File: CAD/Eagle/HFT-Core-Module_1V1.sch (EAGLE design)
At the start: 398 parts, among them Q0521 ABS07-32.768KHZ, Q0811 ABM03B-32.000MHZ, Q0911 ABM3B-16MHZ-10-R50-1-U, T1201 MMBT2222, T1202 MMBT2222, T1203 MMBT2222, U0111 STM32L4Z_144PIN_SMPS, U0431 PAM2305AAB120, U0601 LM4120IM5-3.0, U0611 MAX5217, U0631 CFPT-141-20MHZ, U0641 OPA354, U0701 Si5338, U0801 SX1276, U0901 AX5243, U0911 PE4259, U0921 PE4259, U0991 PE4259, U1101 MCP3911A0-E-SS, U1111 MAX5136AGTG+, U1121 OPA354, U1131 OPA354, U1141 OPA354, U1201 NHD-C0220BIZ_2X20CHARS, U1301 MPU-9250, U1311 MS5607-02BA03, U1321 SHT31-DIS, U1402 SPV1040T, U1501 TS5A23166, U1601 SC189ZSKTRT, U1701 TS5A23166, U1801 TS5A23166, U1901 TS5A23166, X1261 TTE_EN11-HSM, X1401 WIRE-TO-BOARD_5MM08_1X02, X2001 MOLEX 105017-0001, X2101 SMA_SMT_AMPHENOL-901-143, SAM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, X2111 SMA_SMT_AMPHENOL-901-143, SAM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, X2201 CUI SJ1-3535NS, X2211 CUI SJ1-3535NS, X2311 2X20/90_1MM27_HARWIN_M50-3202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, X2312 2X20/90_1MM27_HARWIN_M50-3202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, X2321 2X20/90_1MM27_HARWIN_M50-3202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, X2322 2X20/90_1MM27_HARWIN_M50-3202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, X2331 2X20/90_1MM27_HARWIN_M50-3202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, X2332 2X20/90_1MM27_HARWIN_M50-3202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

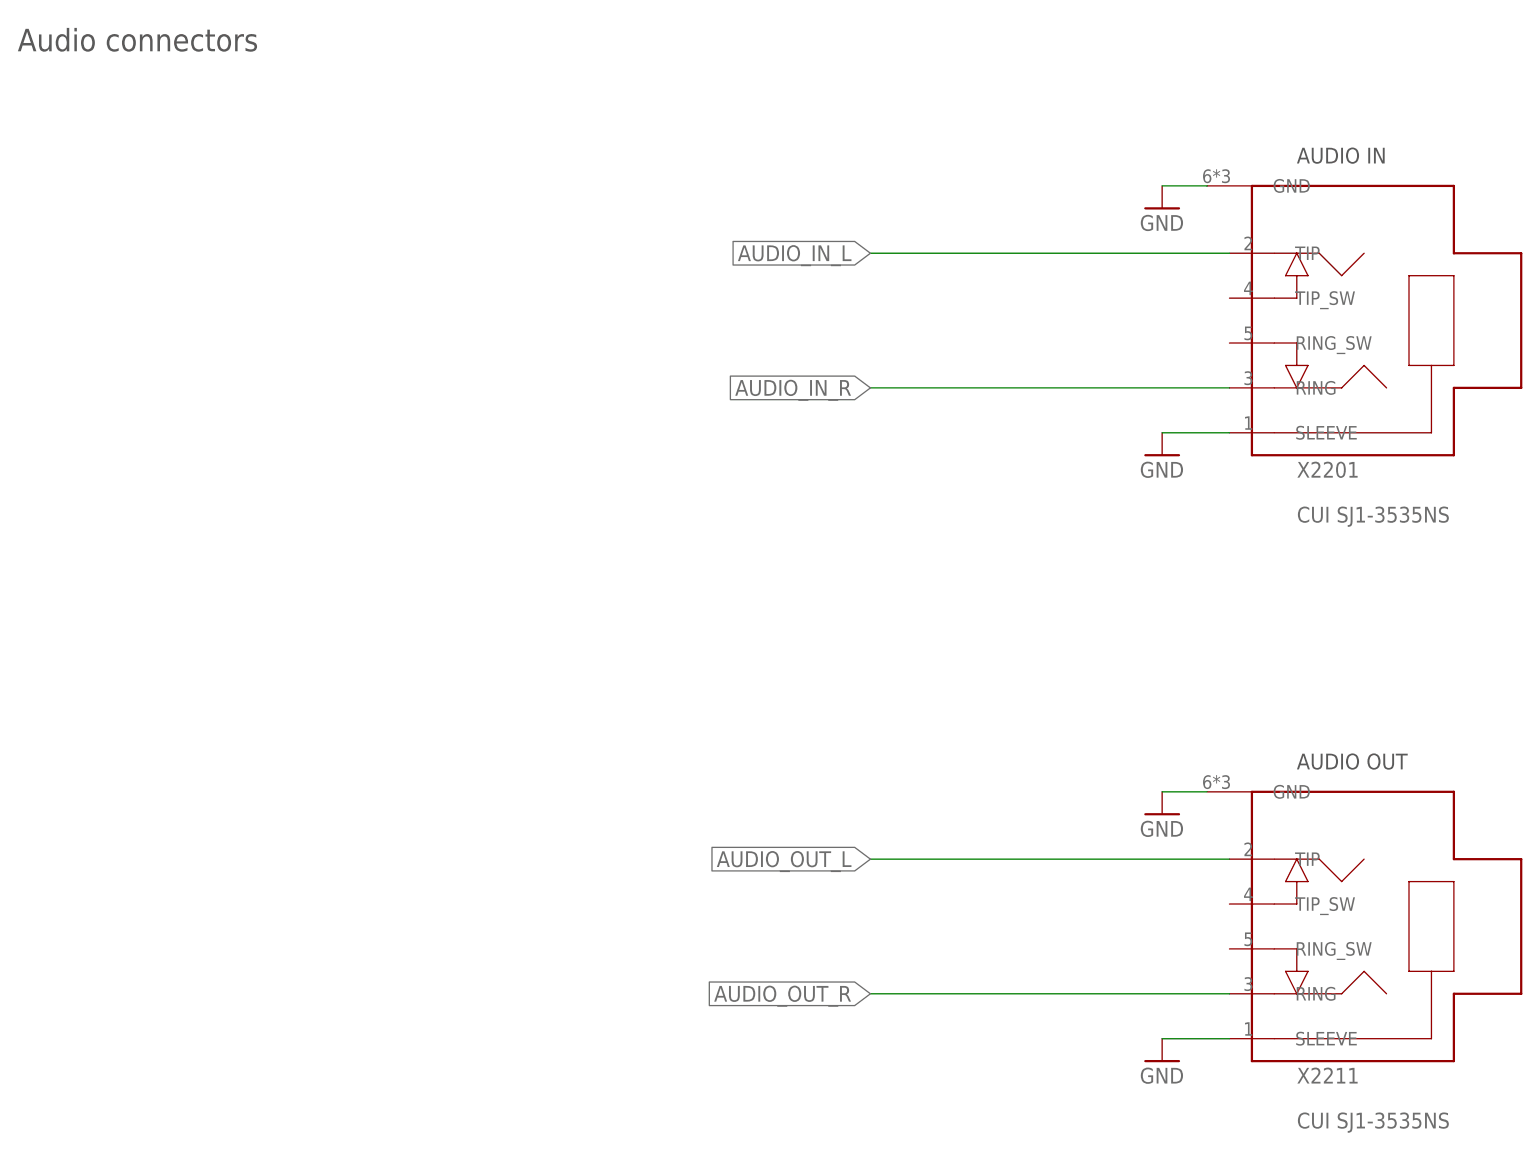
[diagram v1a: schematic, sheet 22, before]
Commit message: HW_1V1 - CAD/Eagle - LCD, Audio jacks and Rotary encoder corrected
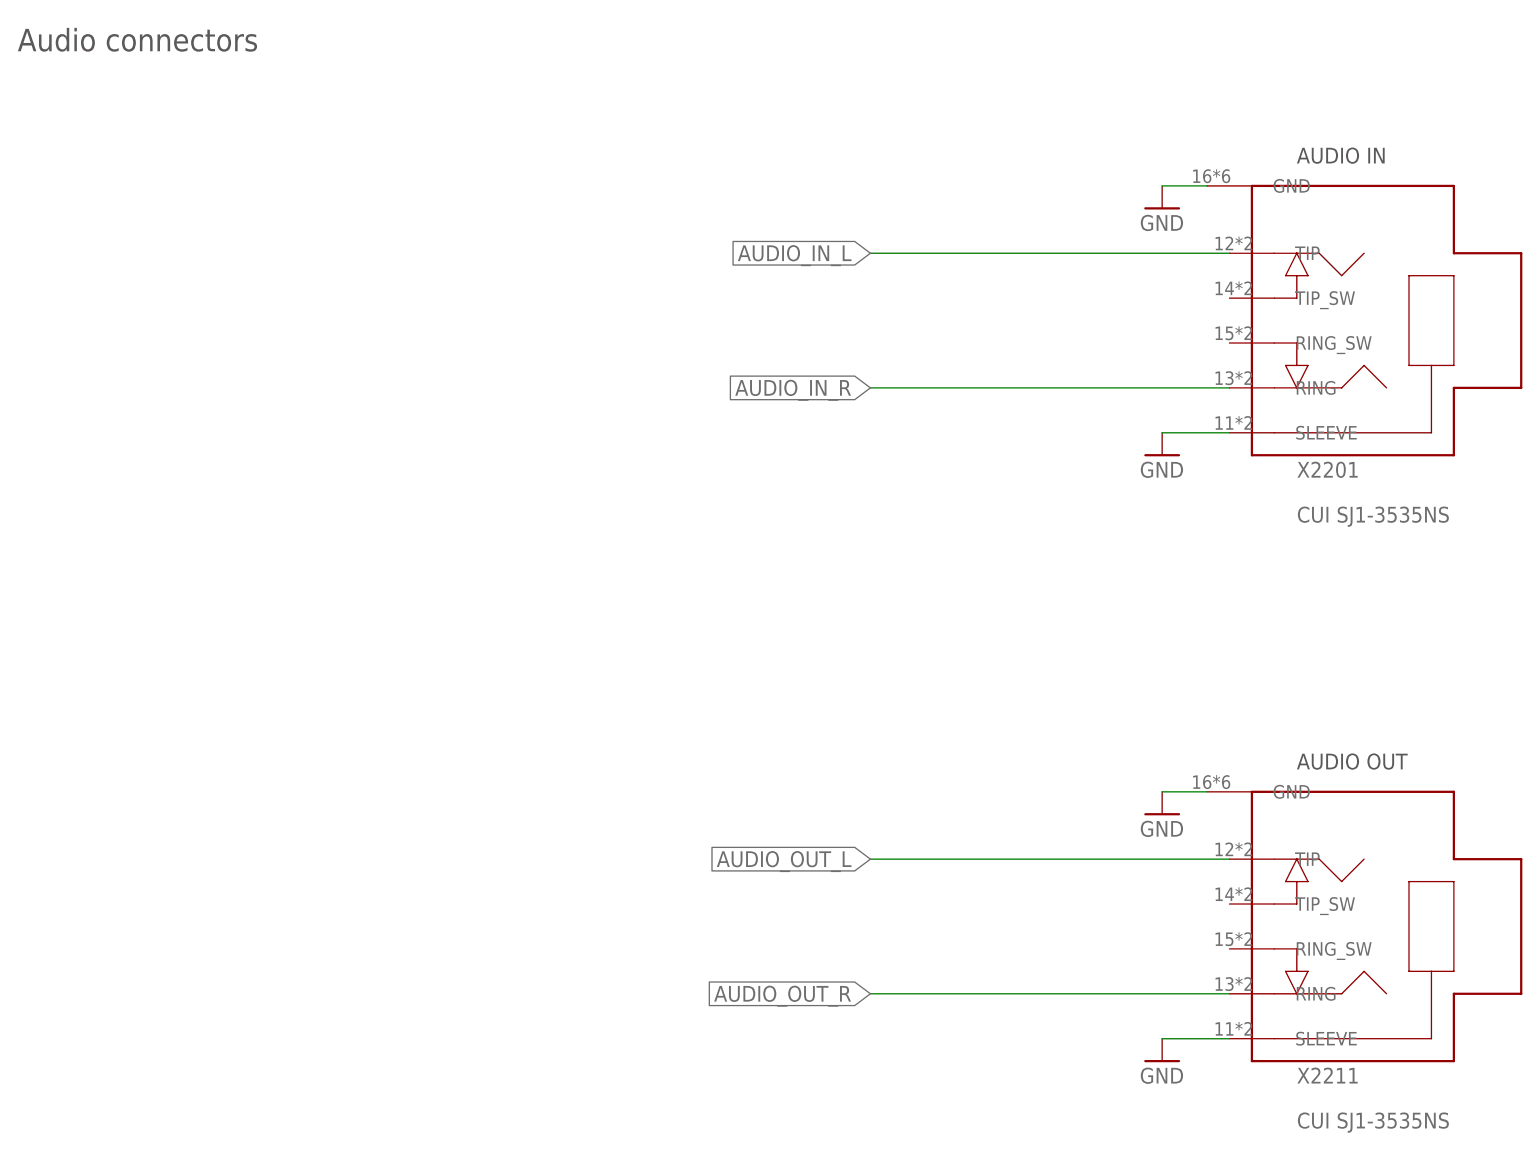
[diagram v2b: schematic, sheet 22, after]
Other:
- moved on the sheet: U1201, X2201, X2211

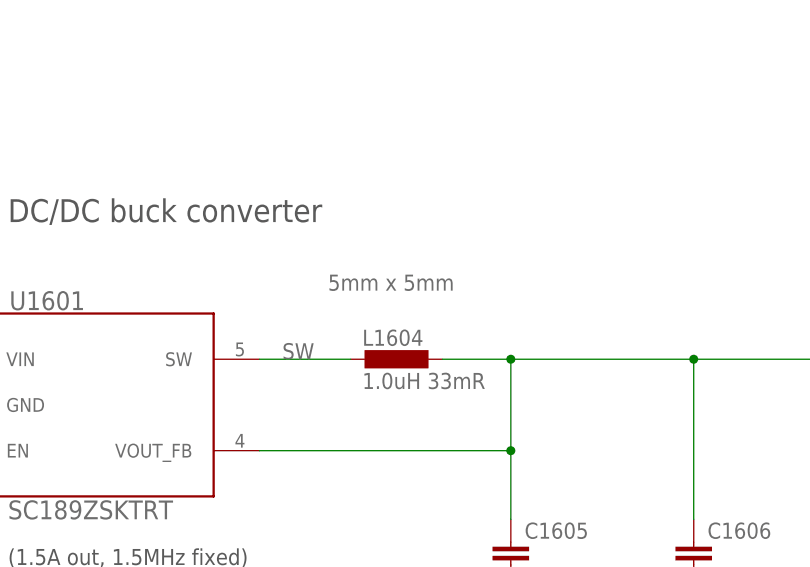
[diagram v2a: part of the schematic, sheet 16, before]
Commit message: HW_1V1 - CAD/Eagle - L1604 size reduced to 3mm x 3mm
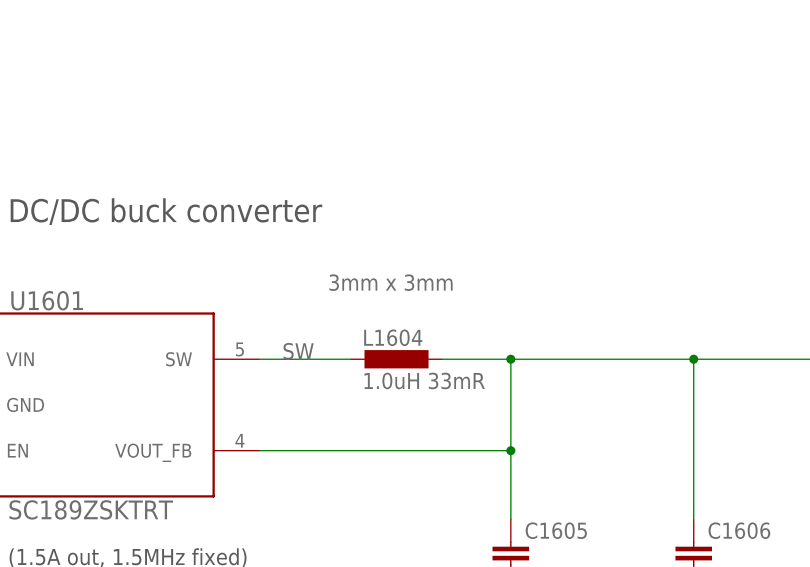
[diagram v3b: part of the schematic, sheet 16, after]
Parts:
- L1604: device rcl:L-EUL5650M -> df4iah_rcl:L-EUL3230M
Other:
- note added: "3mm x 3mm"
- note removed: "5mm x 5mm"
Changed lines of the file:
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@@
 <part name="X2331" library="df4iah_connector" deviceset="2X20/90_1MM27_HARWIN_M50-3202045" device=""/>
 <part name="C1602" library="rcl" deviceset="C-EU" device="C0805" value="47uF"/>
-<part name="L1604" library="rcl" deviceset="L-EU" device="L5650M" value="1.0uH 33mR"/>
+<part name="L1604" library="df4iah_rcl" deviceset="L-EU" device="L3230M" value="1.0uH 33mR"/>
 <part name="C1605" library="rcl" deviceset="C-EU" device="C0603" value="100nF"/>
 <part name="C1606" library="rcl" deviceset="C-EU" device="C0805" value="47uF"/>
@@
 <description>5V -&gt; 3V3</description>
 <plain>
-<text x="139.7" y="104.14" size="1.778" layer="96">5mm x 5mm</text>
+<text x="139.7" y="104.14" size="1.778" layer="96">3mm x 3mm</text>
 <text x="104.14" y="111.76" size="2.54" layer="97" ratio="15">DC/DC buck converter</text>
 <text x="22.86" y="162.56" size="2.54" layer="97" ratio="15">Power converter 5V --&gt; 3.3V</text>

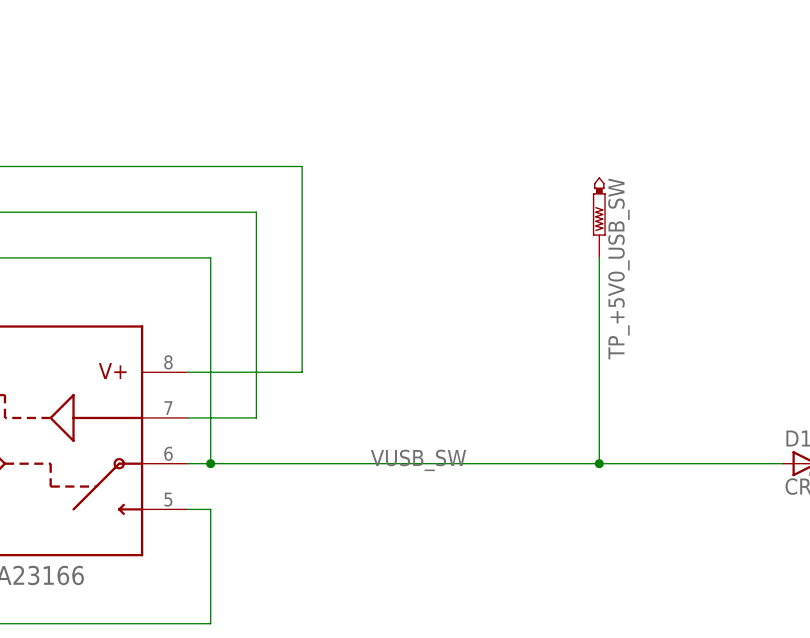
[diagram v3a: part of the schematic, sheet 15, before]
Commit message: HW_1V1 - CAD/Eagle - USB power switch bridged by 50R to enable power-up
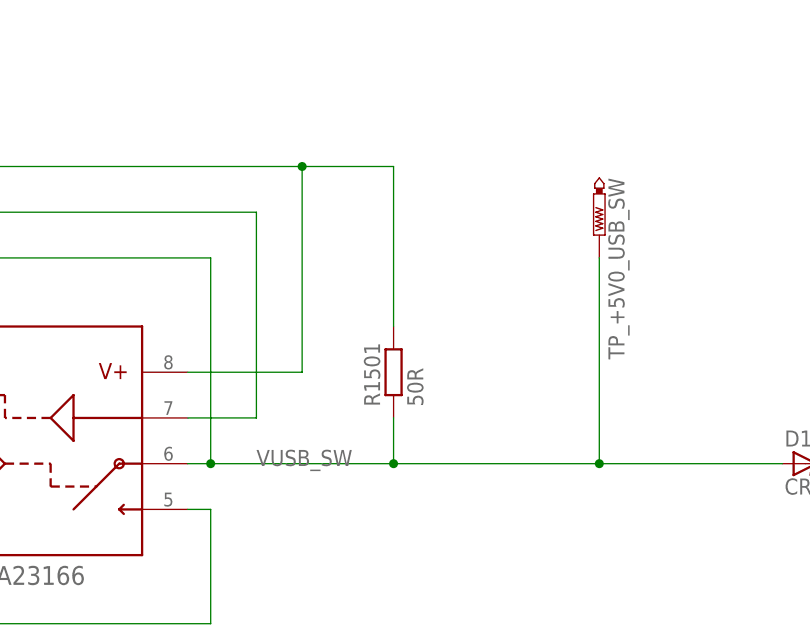
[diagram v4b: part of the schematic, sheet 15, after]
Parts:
- added R1501: 50R, df4iah_rcl:R-EU_R0805
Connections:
- net VDDUSB: now also R1501.2
- net VUSB_SW: now also R1501.1
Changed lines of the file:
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@@
 <part name="R1412" library="rcl" deviceset="R-EU_" device="R0603" value="100kR"/>
 <part name="X1401" library="df4iah_connector" deviceset="WIRE-TO-BOARD_5MM08_1X02" device=""/>
+<part name="R1501" library="df4iah_rcl" deviceset="R-EU_" device="R0805" value="50R"/>
 </parts>
 <sheets>
@@
 <instance part="C1501" gate="G$1" x="68.58" y="71.12"/>
 <instance part="R1502" gate="G$1" x="83.82" y="71.12" rot="R90"/>
+<instance part="R1501" gate="G$1" x="154.94" y="96.52" rot="R90"/>
 </instances>
 <busses>
@@
 <wire x1="198.12" y1="86.36" x2="177.8" y2="86.36" width="0.1524" layer="91"/>
 <pinref part="D1501" gate="G$1" pin="A"/>
-<label x="152.4" y="86.106" size="1.778" layer="95"/>
-<wire x1="177.8" y1="86.36" x2="134.62" y2="86.36" width="0.1524" layer="91"/>
+<label x="139.7" y="86.106" size="1.778" layer="95"/>
+<wire x1="177.8" y1="86.36" x2="154.94" y2="86.36" width="0.1524" layer="91"/>
+<wire x1="154.94" y1="86.36" x2="134.62" y2="86.36" width="0.1524" layer="91"/>
 <wire x1="134.62" y1="109.22" x2="134.62" y2="86.36" width="0.1524" layer="91"/>
 <wire x1="134.62" y1="109.22" x2="93.98" y2="109.22" width="0.1524" layer="91"/>
@@
 <wire x1="177.8" y1="86.36" x2="177.8" y2="109.22" width="0.1524" layer="91"/>
 <junction x="177.8" y="86.36"/>
+<pinref part="R1501" gate="G$1" pin="1"/>
+<wire x1="154.94" y1="86.36" x2="154.94" y2="91.44" width="0.1524" layer="91"/>
+<junction x="154.94" y="86.36"/>
 </segment>
 </net>
@@
 <wire x1="68.58" y1="96.52" x2="68.58" y2="73.66" width="0.1524" layer="91"/>
 <junction x="68.58" y="96.52"/>
+<wire x1="144.78" y1="119.38" x2="154.94" y2="119.38" width="0.1524" layer="91"/>
+<pinref part="R1501" gate="G$1" pin="2"/>
+<wire x1="154.94" y1="119.38" x2="154.94" y2="101.6" width="0.1524" layer="91"/>
+<junction x="144.78" y="119.38"/>
 </segment>
 </net>

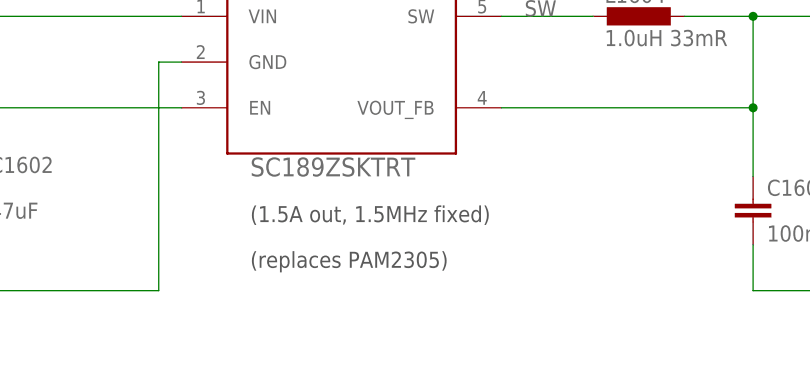
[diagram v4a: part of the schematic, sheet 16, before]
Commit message: HW_1V1 - CAD/Eagle - notice added about current consumption of DcDc converters
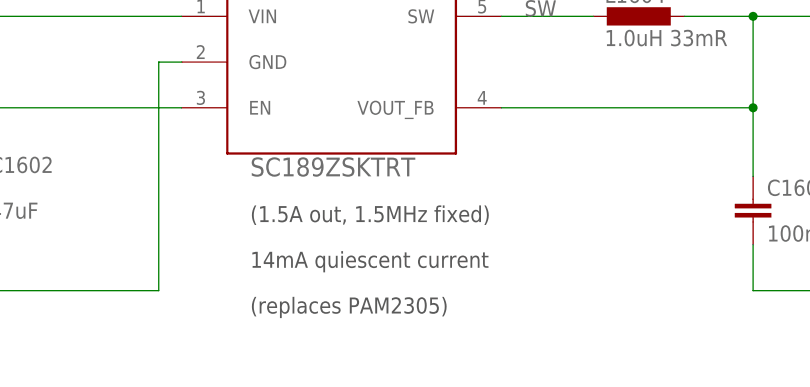
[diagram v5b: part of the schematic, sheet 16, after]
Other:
- note added: "12mA Start-up mode 2mA MPPT mode"
- note added: "14mA quiescent current"
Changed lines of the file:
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@@
 <text x="30.48" y="139.7" size="1.778" layer="97">MCU_VSOL_TIMCAP</text>
 <text x="10.16" y="81.28" size="1.778" layer="97">Solar connector</text>
+<text x="86.36" y="78.74" size="1.778" layer="97">12mA Start-up mode
+ 2mA MPPT mode</text>
 </plain>
 <instances>
@@
 <text x="22.86" y="162.56" size="2.54" layer="97" ratio="15">Power converter 5V --&gt; 3.3V</text>
 <text x="104.14" y="73.66" size="1.778" layer="97">(1.5A out, 1.5MHz fixed)</text>
-<text x="104.14" y="68.58" size="1.778" layer="97">(replaces PAM2305)</text>
+<text x="104.14" y="68.58" size="1.778" layer="97">14mA quiescent current</text>
+<text x="104.14" y="63.5" size="1.778" layer="97">(replaces PAM2305)</text>
 </plain>
 <instances>
